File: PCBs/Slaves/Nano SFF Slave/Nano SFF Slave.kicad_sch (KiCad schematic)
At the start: 52 parts, among them J1 Screw_Terminal_01x02, J10 AVR-ISP-6, J11 Conn_01x06_Female, J12 Screw_Terminal_01x02, J13 Screw_Terminal_01x02, J14 Screw_Terminal_01x02, J15 Screw_Terminal_01x02, J16 Screw_Terminal_01x02, J2 Screw_Terminal_01x02, J3 Screw_Terminal_01x02, J4 Screw_Terminal_01x02, J5 Screw_Terminal_01x02, J6 Screw_Terminal_01x02, J7 Screw_Terminal_01x02, J8 Screw_Terminal_01x02, J9 Screw_Terminal_01x02, SW1 SW_DIP_x02, SW2 SW_DIP_x02, SW3 SW_MEC_5E, U1 ATmega328P-AU, U2 MAX487ESA+T, U3 ULN2003A, U4 MAX487CPA+, U5 AMS1117-5.0, Y1 Crystal_GND24

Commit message: Cleaned up PCB
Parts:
- J1, J12, J13, J14, J15, J16, J2, J3, J4, J5, J6, J7, J8, J9: LCSC C8404 -> C557685
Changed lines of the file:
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@@
       (effects (font (size 1.27 1.27)) hide)
     )
-    (property "LCSC" "C8404" (id 4) (at 271.78 116.84 0)
+    (property "LCSC" "C557685" (id 4) (at 271.78 116.84 0)
       (effects (font (size 1.27 1.27)) hide)
     )
@@
   (symbol (lib_id "power:GND") (at 209.55 53.34 90) (unit 1)
     (in_bom yes) (on_board yes) (fields_autoplaced)
-    (property "Reference" "#PWR?" (id 0) (at 215.9 53.34 0)
+    (property "Reference" "#PWR0109" (id 0) (at 215.9 53.34 0)
       (effects (font (size 1.27 1.27)) hide)
     )
@@
       (effects (font (size 1.27 1.27)) hide)
     )
-    (property "LCSC" "C8404" (id 4) (at 229.87 85.09 0)
+    (property "LCSC" "C557685" (id 4) (at 229.87 85.09 0)
       (effects (font (size 1.27 1.27)) hide)
     )
@@
       (effects (font (size 1.27 1.27)) hide)
     )
-    (property "LCSC" "C8404" (id 4) (at 271.78 111.76 0)
+    (property "LCSC" "C557685" (id 4) (at 271.78 111.76 0)
       (effects (font (size 1.27 1.27)) hide)
     )
@@
       (effects (font (size 1.27 1.27)) hide)
     )
-    (property "LCSC" "C8404" (id 4) (at 204.47 74.93 0)
+    (property "LCSC" "C557685" (id 4) (at 204.47 74.93 0)
       (effects (font (size 1.27 1.27)) hide)
     )
@@
       (effects (font (size 1.27 1.27)) hide)
     )
-    (property "LCSC" "C8404" (id 4) (at 229.87 95.25 0)
+    (property "LCSC" "C557685" (id 4) (at 229.87 95.25 0)
       (effects (font (size 1.27 1.27)) hide)
     )
@@
       (effects (font (size 1.27 1.27)) hide)
     )
-    (property "LCSC" "C8404" (id 4) (at 204.47 80.01 0)
+    (property "LCSC" "C557685" (id 4) (at 204.47 80.01 0)
       (effects (font (size 1.27 1.27)) hide)
     )
@@
       (effects (font (size 1.27 1.27)) hide)
     )
-    (property "LCSC" "C8404" (id 4) (at 229.87 90.17 0)
+    (property "LCSC" "C557685" (id 4) (at 229.87 90.17 0)
       (effects (font (size 1.27 1.27)) hide)
     )
@@
       (effects (font (size 1.27 1.27)) hide)
     )
-    (property "LCSC" "C8404" (id 4) (at 204.47 119.38 0)
+    (property "LCSC" "C557685" (id 4) (at 204.47 119.38 0)
       (effects (font (size 1.27 1.27)) hide)
     )
@@
       (effects (font (size 1.27 1.27)) hide)
     )
-    (property "LCSC" "C8404" (id 4) (at 204.47 90.17 0)
+    (property "LCSC" "C557685" (id 4) (at 204.47 90.17 0)
       (effects (font (size 1.27 1.27)) hide)
     )
@@
       (effects (font (size 1.27 1.27)) hide)
     )
-    (property "LCSC" "C8404" (id 4) (at 229.87 74.93 0)
+    (property "LCSC" "C557685" (id 4) (at 229.87 74.93 0)
       (effects (font (size 1.27 1.27)) hide)
     )
@@
       (effects (font (size 1.27 1.27)) hide)
     )
-    (property "LCSC" "C8404" (id 4) (at 229.87 69.85 0)
+    (property "LCSC" "C557685" (id 4) (at 229.87 69.85 0)
       (effects (font (size 1.27 1.27)) hide)
     )
@@
       (effects (font (size 1.27 1.27)) hide)
     )
-    (property "LCSC" "C8404" (id 4) (at 229.87 80.01 0)
+    (property "LCSC" "C557685" (id 4) (at 229.87 80.01 0)
       (effects (font (size 1.27 1.27)) hide)
     )
@@
       (effects (font (size 1.27 1.27)) hide)
     )
-    (property "LCSC" "C8404" (id 4) (at 215.9 119.38 0)
+    (property "LCSC" "C557685" (id 4) (at 215.9 119.38 0)
       (effects (font (size 1.27 1.27)) hide)
     )
@@
       (effects (font (size 1.27 1.27)) hide)
     )
-    (property "LCSC" "C8404" (id 4) (at 204.47 85.09 0)
+    (property "LCSC" "C557685" (id 4) (at 204.47 85.09 0)
       (effects (font (size 1.27 1.27)) hide)
     )
@@
       (reference "#PWR0108") (unit 1) (value "GND") (footprint "")
     )
+    (path "/0b79672f-4d98-4fc7-9f12-b9b83ab0f075"
+      (reference "#PWR0109") (unit 1) (value "GND") (footprint "")
+    )
     (path "/cd316508-8228-49f2-8377-87d2467c6ee5"
       (reference "#PWR0111") (unit 1) (value "GND") (footprint "")
@@
       (reference "#PWR0145") (unit 1) (value "+5V") (footprint "")
     )
-    (path "/0b79672f-4d98-4fc7-9f12-b9b83ab0f075"
-      (reference "#PWR?") (unit 1) (value "GND") (footprint "")
-    )
     (path "/df5accf7-095f-40f9-b40a-a9b9e4c1a11a"

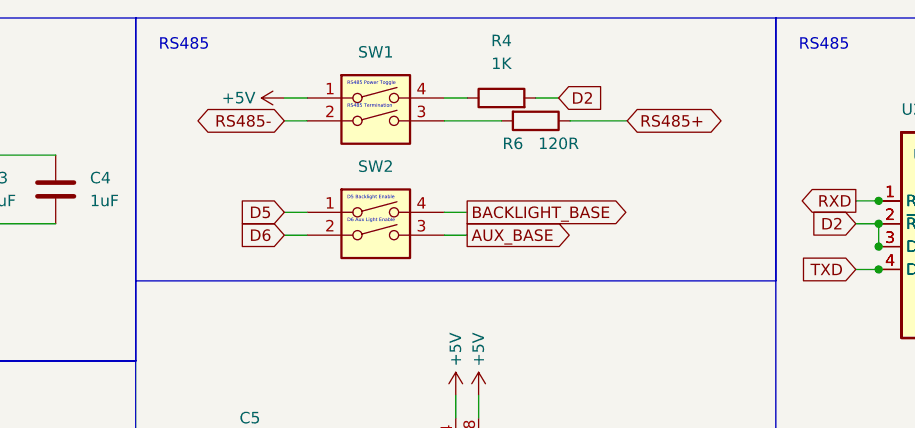
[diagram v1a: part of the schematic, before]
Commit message: Updated Nano SFF Slave RS485 Switch and Silkscreen
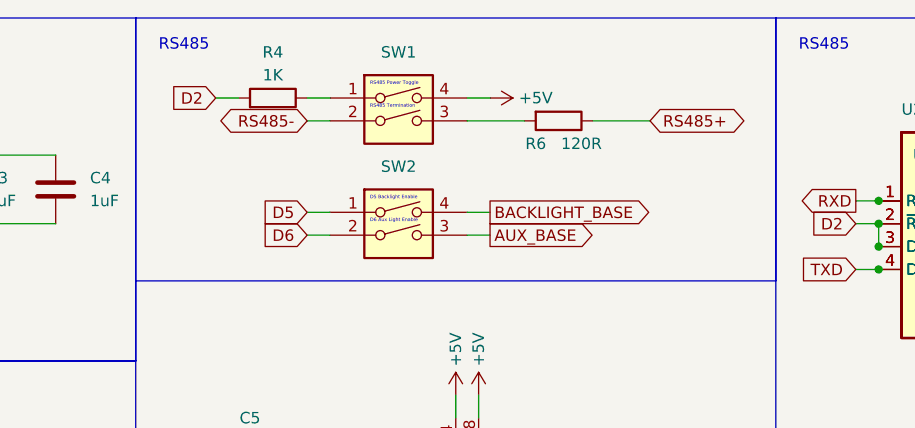
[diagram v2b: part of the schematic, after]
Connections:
- net +5V: now also SW1.4; no longer SW1.1
- net at R4.1: now also SW1.1; no longer SW1.4
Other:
- moved on the sheet: R4, R6, SW1, SW2

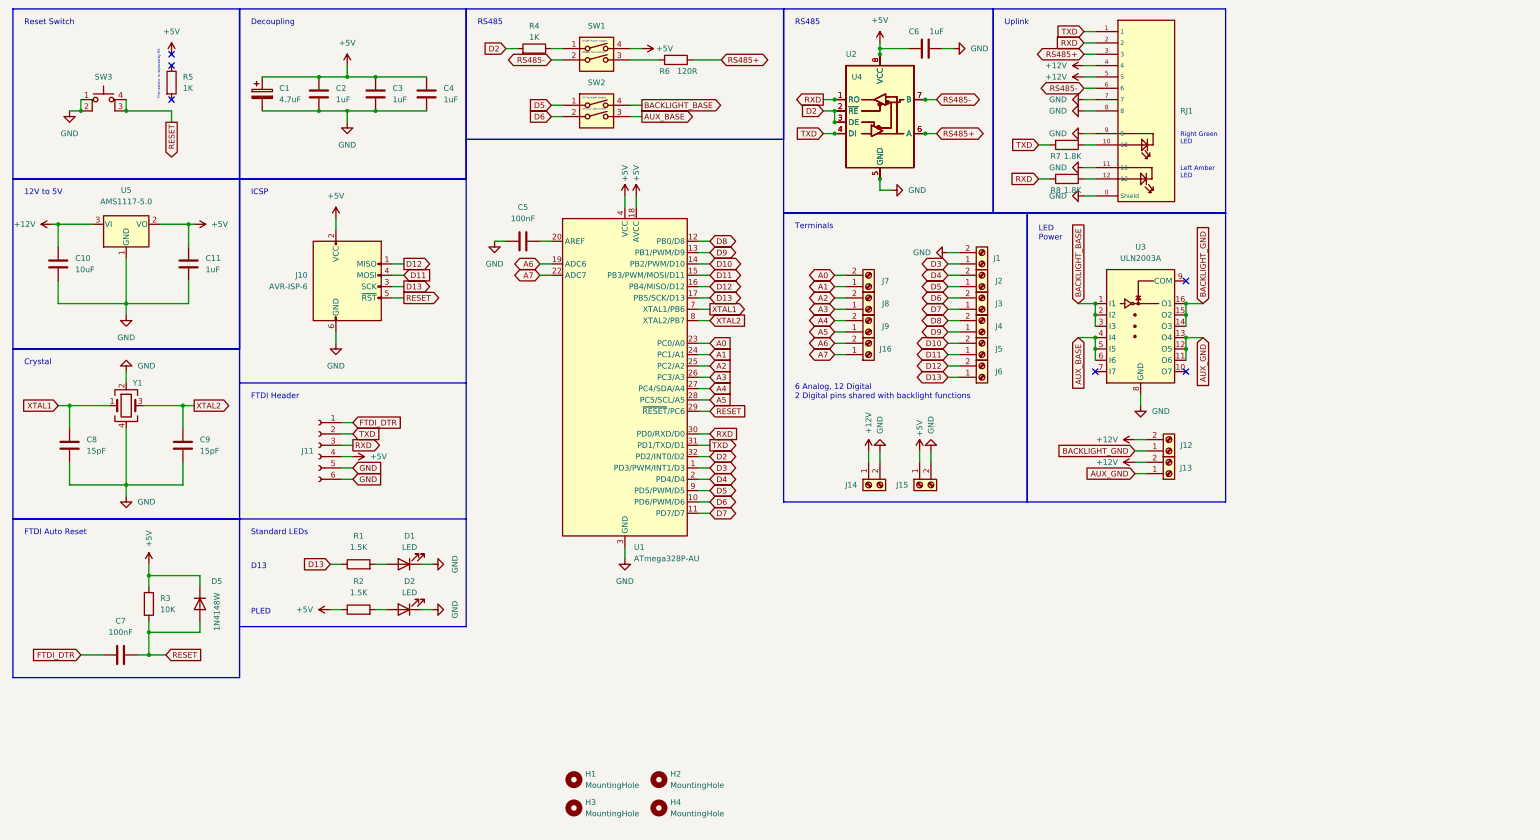
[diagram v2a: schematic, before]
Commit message: Nano SFF with DS4560S-AR+ hotplug protection (Not Orderable)
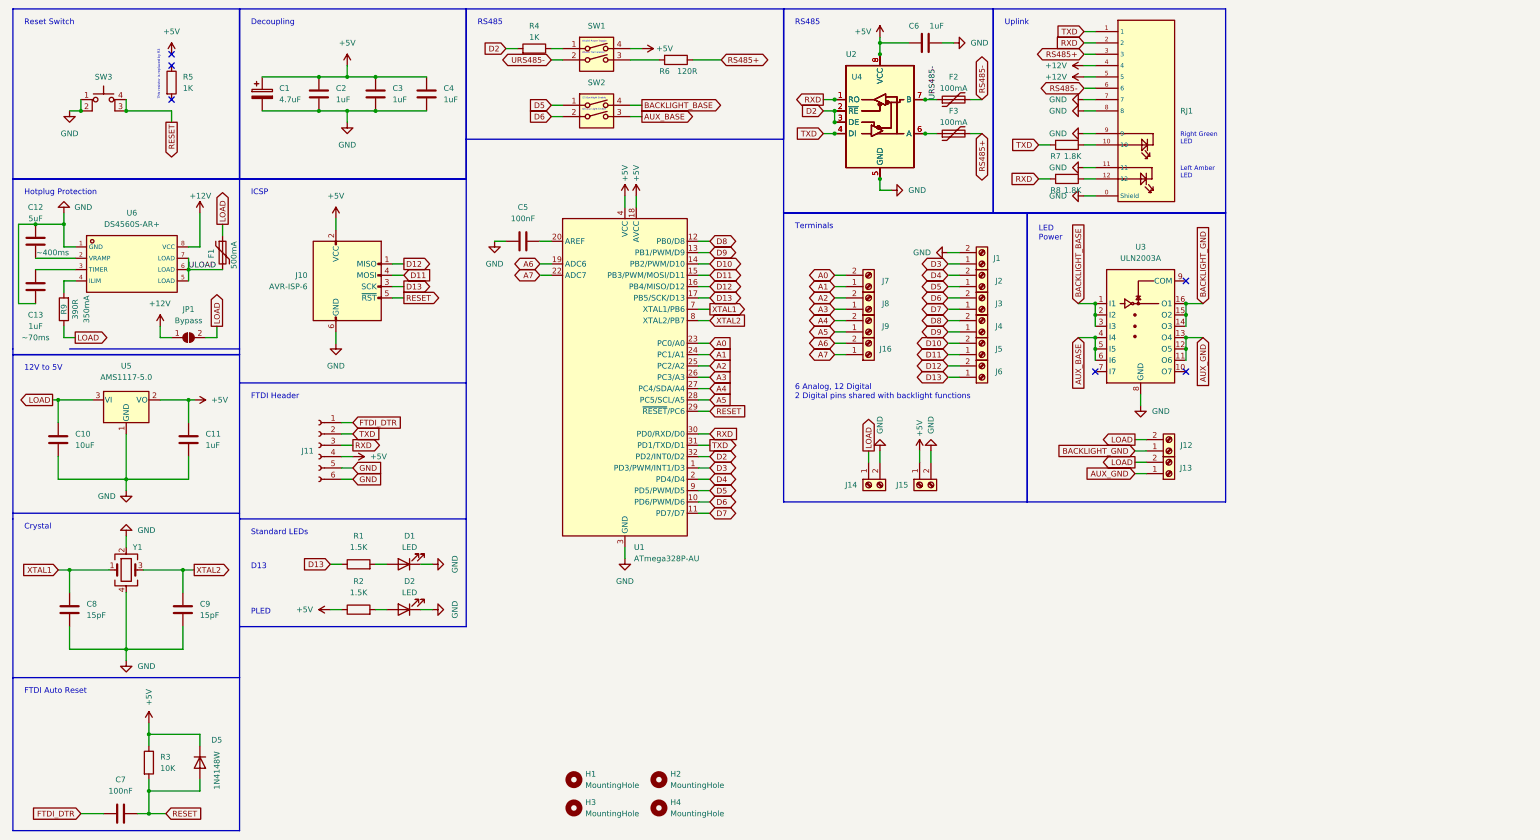
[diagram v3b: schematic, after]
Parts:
- added C12: 5uF, A10 KiCad Libraries:C0402, symbol Device:C
- added C13: 1uF, A10 KiCad Libraries:C0402, symbol Device:C
- added F1: 500mA, Fuse:Fuse_1206_3216Metric, symbol Device:Polyfuse
- added F2, F3: 100mA, Fuse:Fuse_0603_1608Metric, symbol Device:Polyfuse
- added JP1: Bypass, Jumper:SolderJumper-2_P1.3mm_Open_RoundedPad1.0x1.5mm, symbol Jumper:SolderJumper_2_Open
- added R9: 390R, Resistor_SMD:R_0805_2012Metric, symbol Device:R
- added U6: DS4560S-AR+, A10 KiCad Libraries:SOIC-8_L4.9-W3.9-P1.27-LS6.0-BL, symbol A10:DS4560S-AR+
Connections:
- net +12V: now also JP1.1 (A), U6.8 (VCC); no longer C10.1, J12.2 (Pin_2), J13.2 (Pin_2), J14.1 (Pin_1), U5.3 (VI)
- net GND: now also C12.1, C13.2, U6.1 (GND)
- net RS485+: now also F3.2; no longer U2.6 (A), U4.6 (A)
- net RS485-: now also F2.2; no longer SW1.2, U2.7 (B), U4.7 (B)
- new net: F3.1, U2.6 (A), U4.6 (A)
- new net: C12.2, U6.2 (VRAMP)
- new net: C13.1, U6.3 (TIMER)
- new net: R9.2, U6.4 (ILIM)
- new net LOAD: C10.1, F1.1, J12.2 (Pin_2), J13.2 (Pin_2), J14.1 (Pin_1), JP1.2 (B), R9.1, U5.3 (VI)
- new net ULOAD: F1.2, U6.5 (LOAD), U6.6 (LOAD), U6.7 (LOAD)
- new net URS485-: F2.1, SW1.2, U2.7 (B), U4.7 (B)
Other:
- note added: "Hotplug Protection"
- moved on the sheet: C10, C11, C6, C7, C8, C9, D5, R3, U5, Y1

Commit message: Added new components
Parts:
- removed C12: 5uF, A10 KiCad Libraries:C0402, symbol Device:C
- removed C13: 1uF, A10 KiCad Libraries:C0402, symbol Device:C
- removed F1: 500mA, Fuse:Fuse_1206_3216Metric, symbol Device:Polyfuse
- removed R9: 390R, Resistor_SMD:R_0805_2012Metric, symbol Device:R
- removed U6: DS4560S-AR+, A10 KiCad Libraries:SOIC-8_L4.9-W3.9-P1.27-LS6.0-BL, symbol A10:DS4560S-AR+
- added D?: SM712_SOT23, Package_TO_SOT_SMD:SOT-23, symbol Diode:SM712_SOT23
- added U? (x2): TISP4240M3BJR-S, footprint:DO-214AA_L4.4-W3.6-LS5.3-BI, symbol A10:TISP4240M3BJR-S
- added U? (x2): TBU-CA065-200-WH, footprint:DIO-SMD_3P-L6.5-W4.0-BI, symbol A10:TBU-CA065-200-WH
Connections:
- net +12V: no longer JP1.1 (A)
- net LOAD: no longer JP1.2 (B)
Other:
- moved on the sheet: C10, C11, C7, C8, C9, D5, JP1, R3, U5, Y1

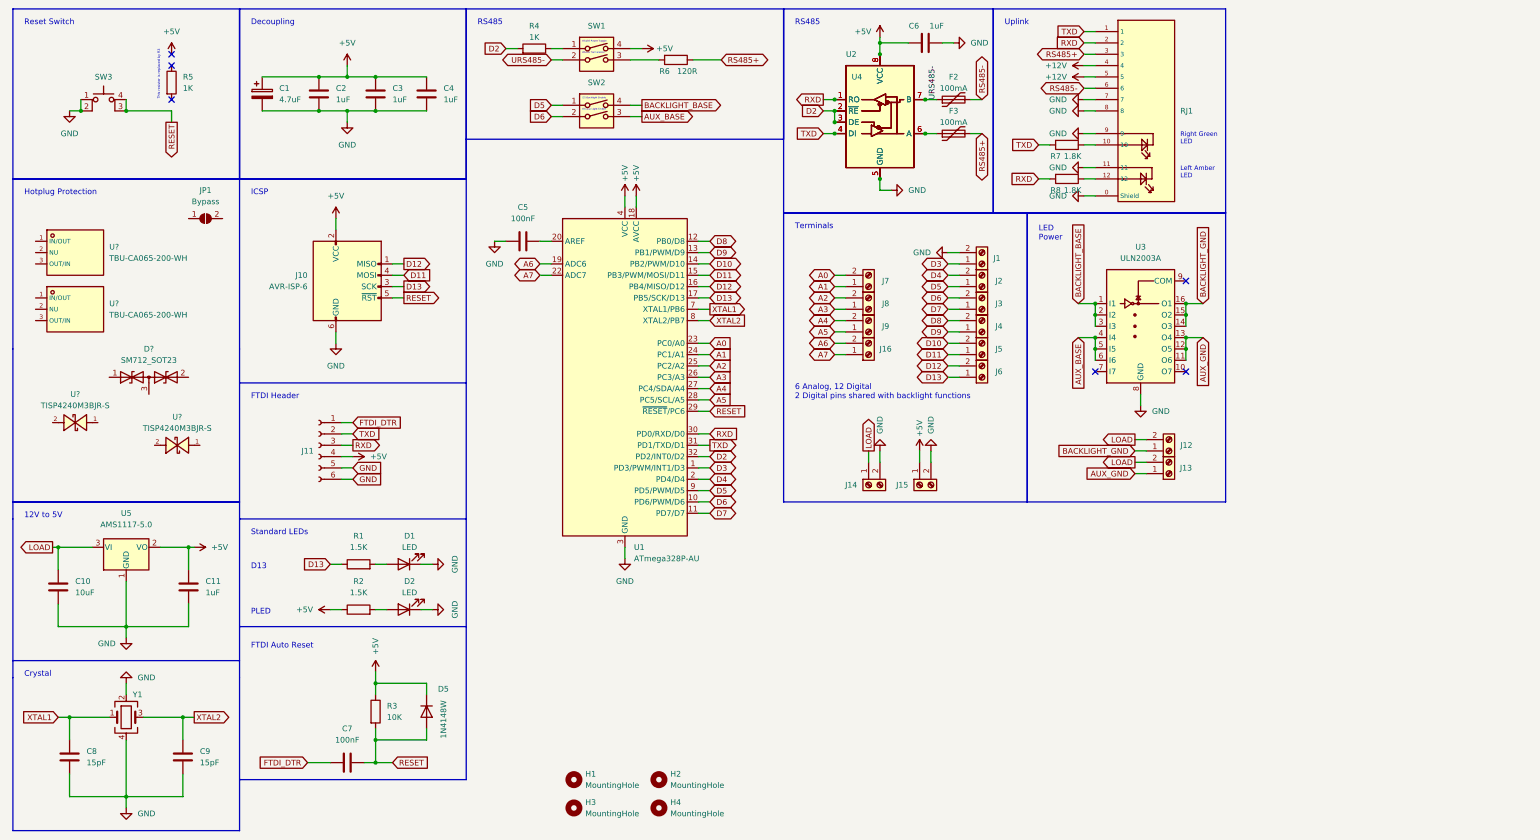
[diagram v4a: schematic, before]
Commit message: Nano SFF With Hotplug and RS485 Protection
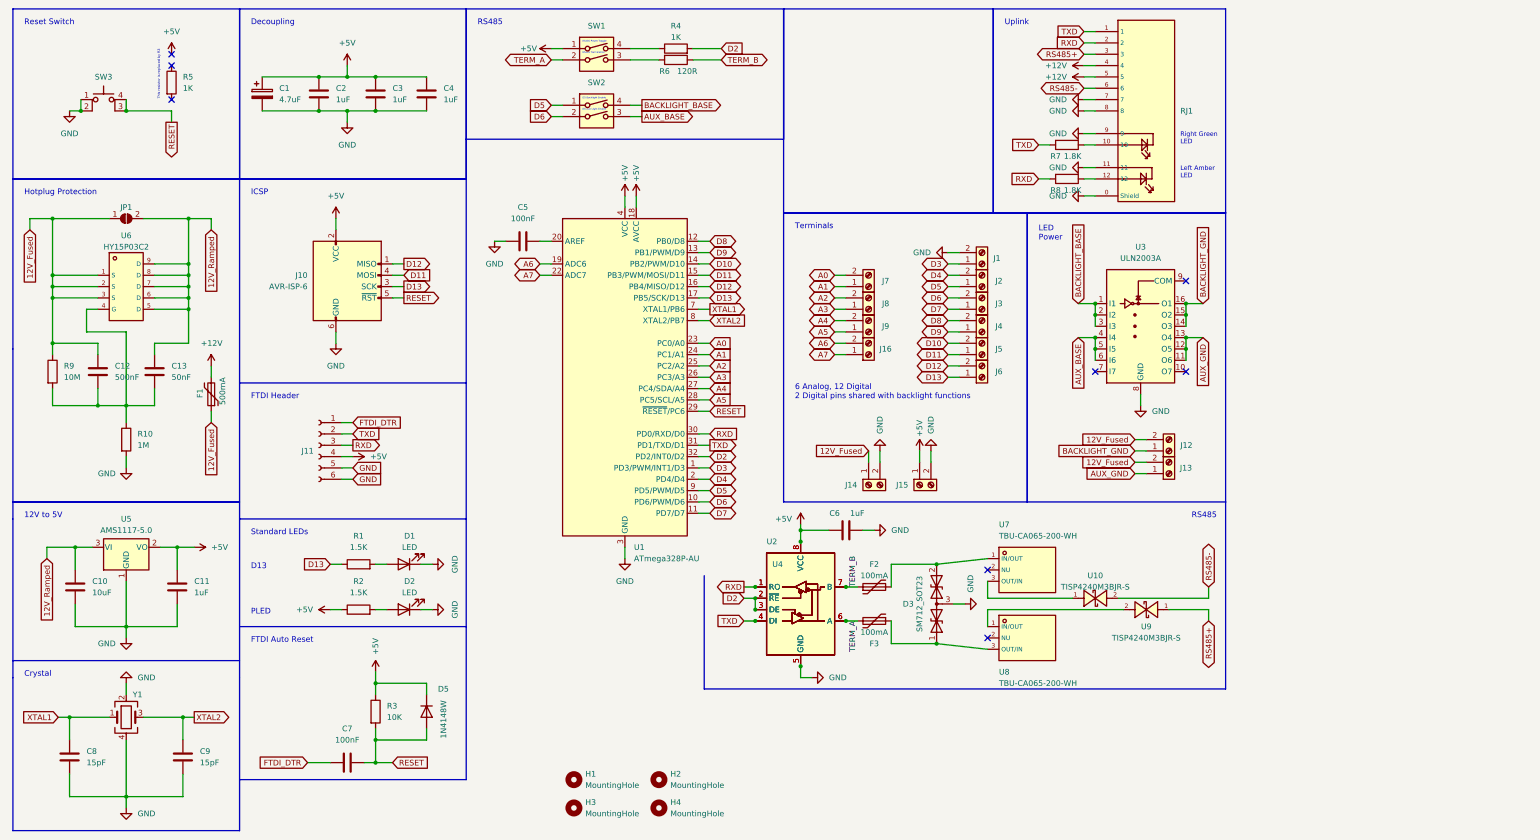
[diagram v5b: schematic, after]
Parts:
- added C12: 500nF, A10 KiCad Libraries:C0402, symbol Device:C
- added C13: 50nF, A10 KiCad Libraries:C0402, symbol Device:C
- added F1: 500mA, Fuse:Fuse_1206_3216Metric, symbol Device:Polyfuse
- added R10: 1M, Resistor_SMD:R_0603_1608Metric, symbol Device:R
- added R9: 10M, Resistor_SMD:R_0603_1608Metric, symbol Device:R
- added U6: HY15P03C2, A10 KiCad Libraries:DFN-8_L5.9-W5.2-P1.27-LS6.2-BL, symbol A10:HY15P03C2
- JP1: value Bypass -> Solder
- U10, U9: renamed from U?; footprint footprint:DO-214AA_L4.4-W3.6-LS5.3-BI -> A10 KiCad Libraries:DO-214AA_L4.4-W3.6-LS5.3-BI
- U7, U8: renamed from U?; footprint footprint:DIO-SMD_3P-L6.5-W4.0-BI -> A10 KiCad Libraries:DIO-SMD_3P-L6.5-W4.0-BI
- gave numbers to parts that had none: 1
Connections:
- net +12V: now also F1.2
- net +5V: now also SW1.1; no longer SW1.4
- net GND: now also D3.3 (common), R10.2
- net RS485+: now also U9.1 (A); no longer F3.2, R6.1
- net RS485-: now also U10.2 (K); no longer F2.2
- net at U9.2 (K): now also U8.1 (IN/OUT)
- net at R4.1: now also SW1.4; no longer SW1.1
- net at U10.1 (A): now also U7.3 (OUT/IN)
- net TERM_A: now reaches U2.6 (A), U4.6 (A)
- net TERM_A: now also F3.2, SW1.2; no longer F3.1
- net at U8.3 (OUT/IN): now also D3.1 (A1), F3.1
- net at D3.2 (A2): now also F2.2, U7.1 (IN/OUT)
- net 12V_Fused: now reaches JP1.1 (A)
- net 12V_Fused: now also J12.2 (Pin_2), J13.2 (Pin_2), J14.1 (Pin_1), C12.1, F1.1, R9.1, U6.1 (S), U6.2 (S), U6.3 (S)
- net 12V_Ramped: now reaches JP1.2 (B)
- net 12V_Ramped: now also C10.1, U5.3 (VI), C13.1, U6.5 (D), U6.6 (D), U6.7 (D), U6.8 (D), U6.9 (D)
- removed net LOAD: C10.1, J12.2 (Pin_2), J13.2 (Pin_2), J14.1 (Pin_1), U5.3 (VI)
- net URS485- renamed TERM_B
- net TERM_B: now also R6.1; no longer SW1.2
- new net: C12.2, C13.2, R10.1, R9.2, U6.4 (G)
- no-connect marks 6 -> 8
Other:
- moved on the sheet: C10, C11, C6, D3, F2, F3, JP1, R4, U10, U2, U4, U7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
